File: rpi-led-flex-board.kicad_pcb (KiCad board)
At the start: 2 copper layers, 70.3 x 35.6 mm, 29 parts, among them J1 TE_1-1734248-5_FLEX, U1 PCA9685BS,118

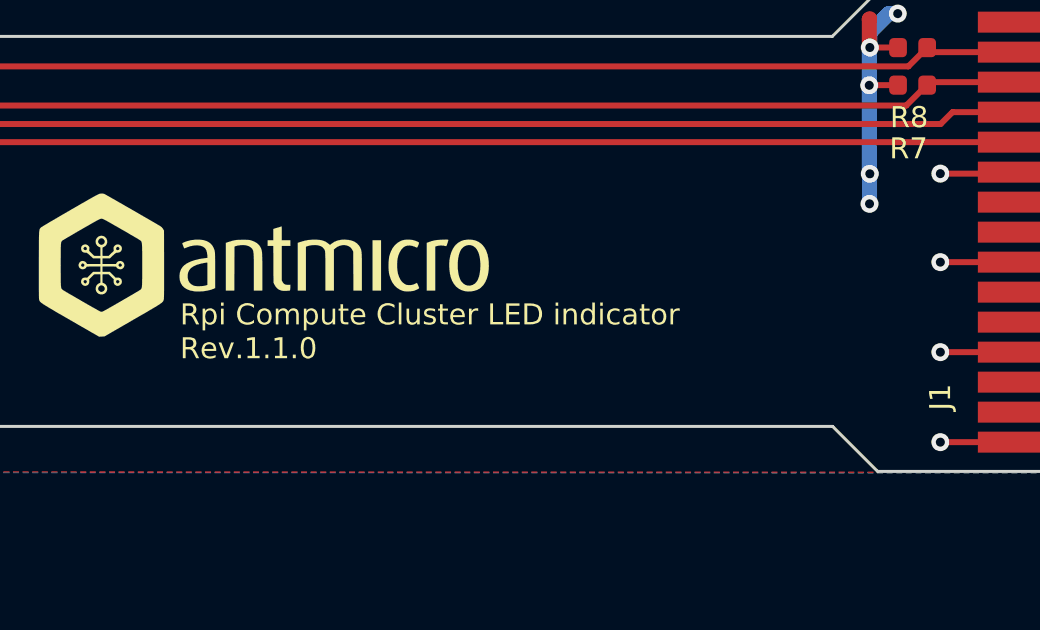
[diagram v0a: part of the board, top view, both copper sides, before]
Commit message: Update naming convention
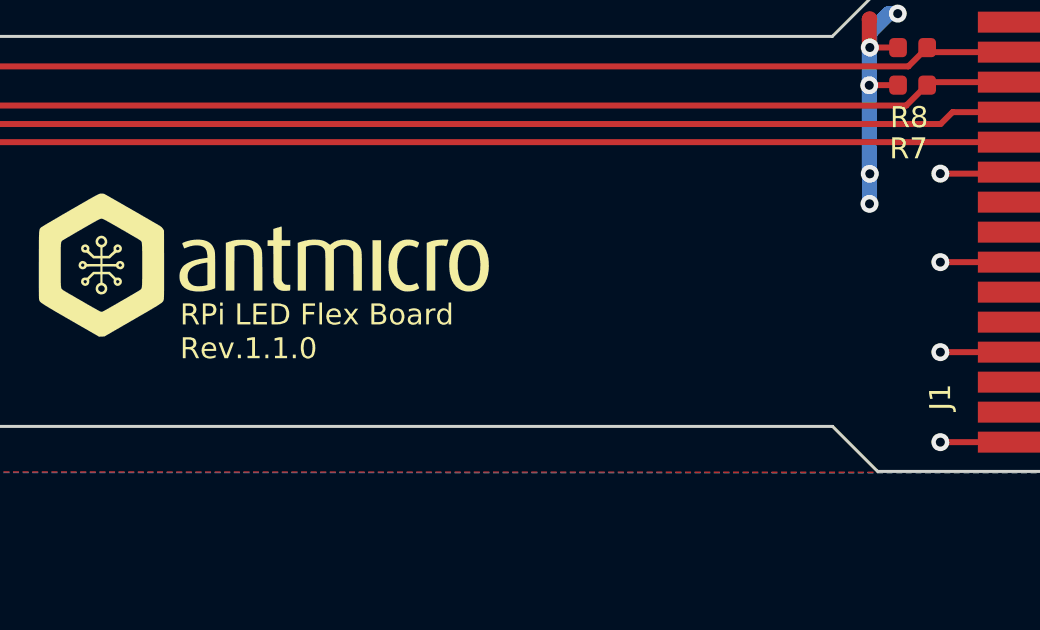
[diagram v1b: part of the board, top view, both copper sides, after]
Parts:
- C1: footprint rpi-compute-cluster-led-indicator-footprints:0402-cap -> rpi-led-flex-board-footprints:0402-cap
- D1, D2, D3, D4, D5: footprint rpi-compute-cluster-led-indicator-footprints:LED_Dual0603 -> rpi-led-flex-board-footprints:LED_Dual0603
- J1: footprint rpi-compute-cluster-led-indicator-footprints:TE_1-1734248-5_FLEX -> rpi-led-flex-board-footprints:TE_1-1734248-5_FLEX
- N1: footprint rpi-compute-cluster-led-indicator-footprints:antmicro-logo_scaled_15mm_silk -> rpi-led-flex-board-footprints:antmicro-logo_scaled_15mm_silk
- N2: footprint rpi-compute-cluster-led-indicator-footprints:OSHW-Logo_5.7x6mm_SilkScreen -> rpi-led-flex-board-footprints:OSHW-Logo_5.7x6mm_SilkScreen
- R1, R10, R11, R12, R13, R14, R15, R16, R17, R18, R19, R2, R3, R4, R5, R6, R7, R8, R9: footprint rpi-compute-cluster-led-indicator-footprints:0402-res -> rpi-led-flex-board-footprints:0402-res
- U1: footprint rpi-compute-cluster-led-indicator-footprints:QFN-28_6x6mm_P0.65mm -> rpi-led-flex-board-footprints:QFN-28_6x6mm_P0.65mm
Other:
- board text added: "RPi LED Flex Board Rev.1.1.0"
- board text removed: "Rpi Compute Cluster LED indicator Rev.1.1.0"
